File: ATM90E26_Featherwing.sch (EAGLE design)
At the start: 60 parts, among them J1 ST-PJ-312, J2 4P-SMD-2.0-90D, J3 4P-SMD-2.0-90D, J4 12V AC, Q1 8.192MHz, U1 ATM90E26, U2 CJT1117-5.0-SOT223

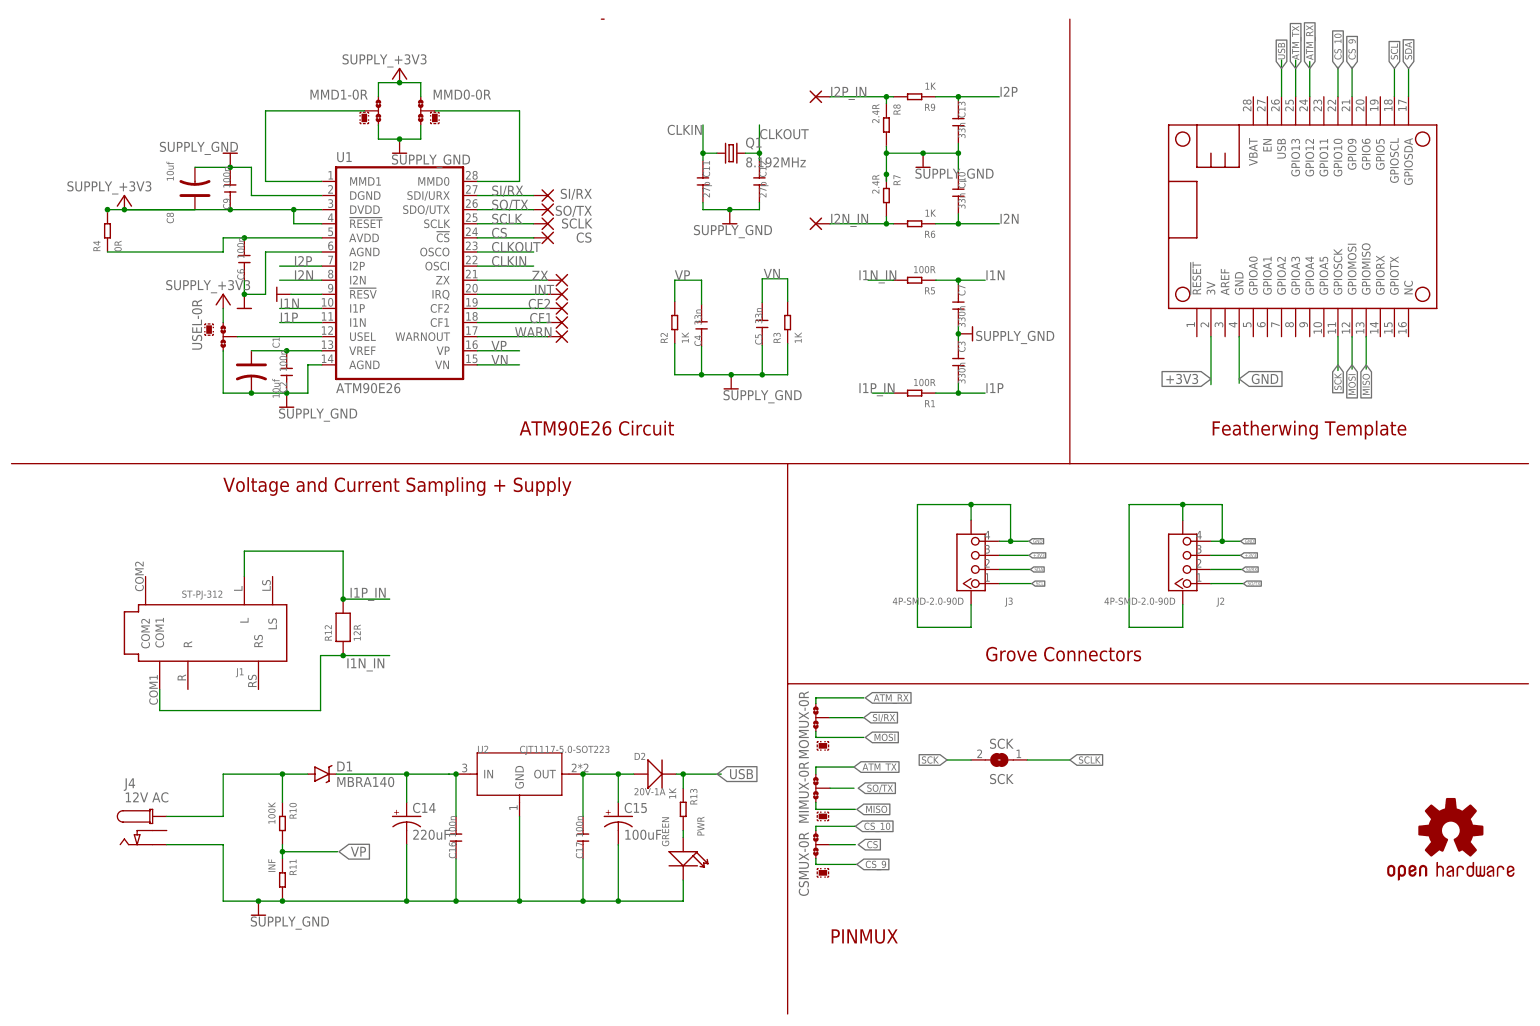
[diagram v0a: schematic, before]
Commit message: Used smaller solder jumpers and finished route, bumped version
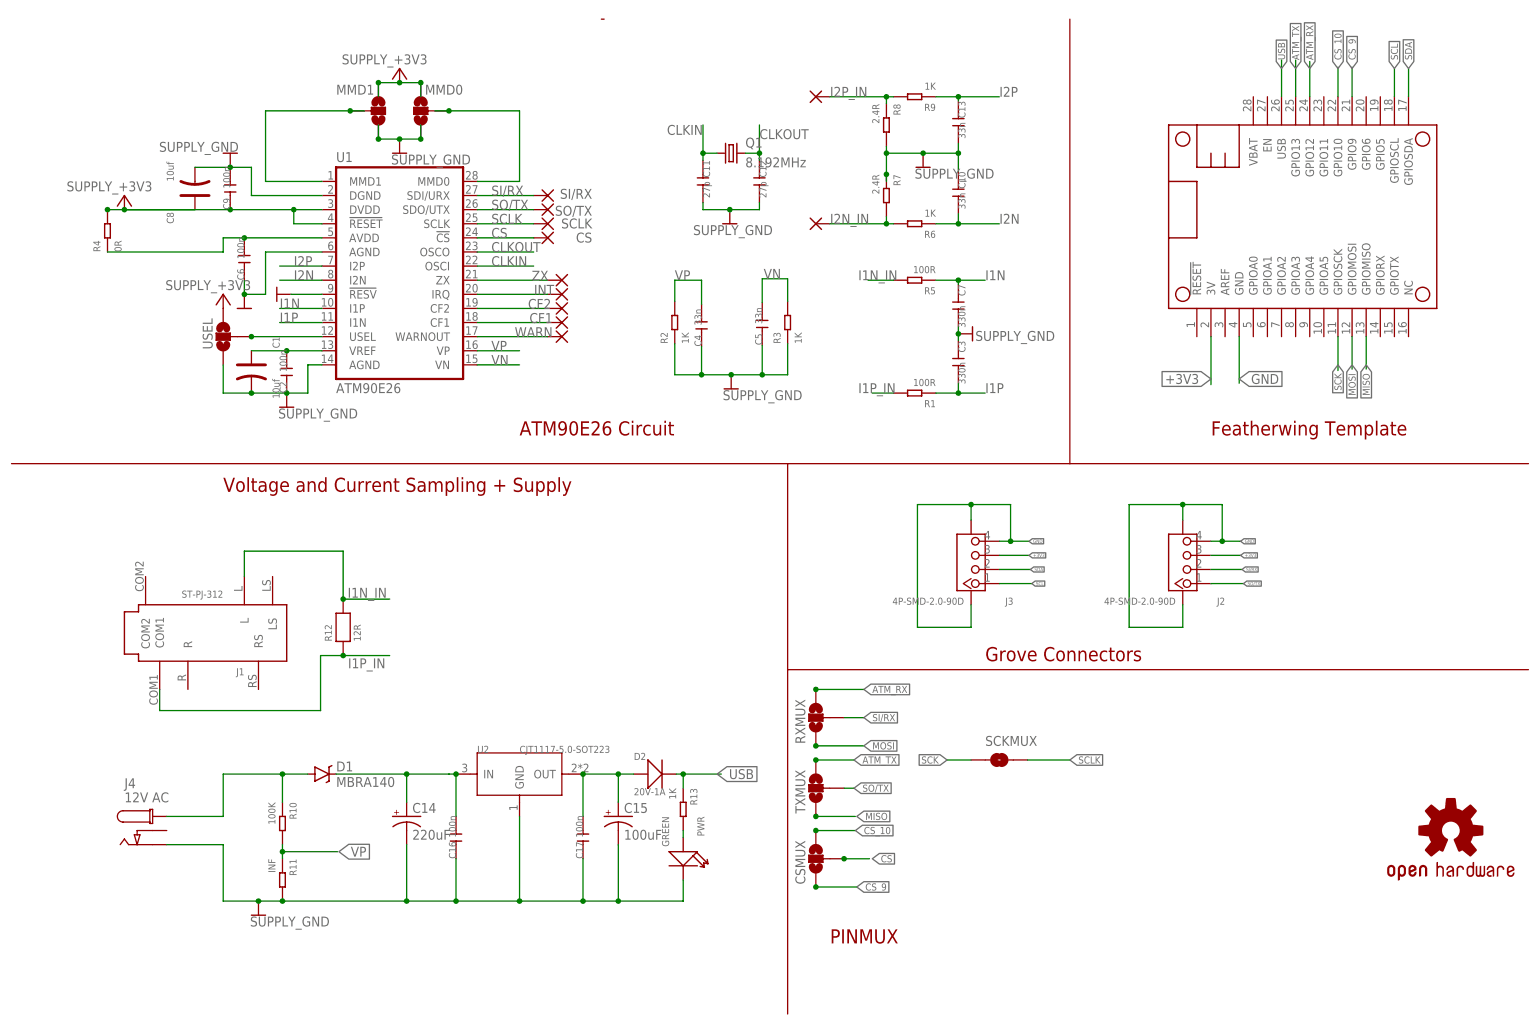
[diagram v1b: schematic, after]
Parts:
- removed MIMUX, MOMUX: 0R-JUMPA, jump-0r-smd:0R-JUMPA
- removed SCK: SCK, jumper:SJ
- added RXMUX, TXMUX: JUMPER-PAD-3-NOYES_SILK, SparkFun-Passives:JUMPER-PAD-3-NOYES_SILK
- added SCKMUX: JUMPER-PAD-2-NOYES_SILK, SparkFun-Passives:JUMPER-PAD-2-NOYES_SILK
- CSMUX: value 0R-JUMPA -> JUMPER-PAD-3-NOYES_SILK; device jump-0r-smd:0R-JUMPA -> SparkFun-Passives:JUMPER-PAD-3-NOYES_SILK
- MMD0, MMD1, USEL: value 0R-JUMPA -> JUMPER-PAD-3-NOFULL_BOX_SILK; device jump-0r-smd:0R-JUMPA -> SparkFun-Passives:JUMPER-PAD-3-NOFULL_BOX_SILK
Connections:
- net +3V3: now also MMD0.3, MMD1.1, USEL.3; no longer MMD0-0R.1, MMD1-0R.3, USEL-0R.1
- net ATM_RX: now also RXMUX.3; no longer MOMUX-0R.1
- net ATM_TX: now also TXMUX.3; no longer MIMUX-0R.1
- net CS: now also CSMUX.2; no longer CSMUX-0R.2
- net CS_10: now also CSMUX.3; no longer CSMUX-0R.1
- net CS_9: now also CSMUX.1; no longer CSMUX-0R.3
- net GND: now also MMD0.1, MMD1.3, USEL.1; no longer MMD0-0R.3, MMD1-0R.1, USEL-0R.3
- net I1N_IN: now also J1.L, R12.2; no longer J1.COM1, R12.1
- net I1P_IN: now also J1.COM1, R12.1; no longer J1.L, R12.2
- net MISO: now also TXMUX.1; no longer MIMUX-0R.3
- net MOSI: now also RXMUX.1; no longer MOMUX-0R.3
- net N$1: now also MMD1.2; no longer MMD1-0R.2
- net N$15: now also USEL.2; no longer USEL-0R.2
- net N$2: now also MMD0.2; no longer MMD0-0R.2
- net SCK: now also SCKMUX.1; no longer SCK.2
- net SCLK: now also SCKMUX.2; no longer SCK.1
- net SI/RX: now also RXMUX.2; no longer MOMUX-0R.2
- net SO/TX: now also TXMUX.2; no longer MIMUX-0R.2

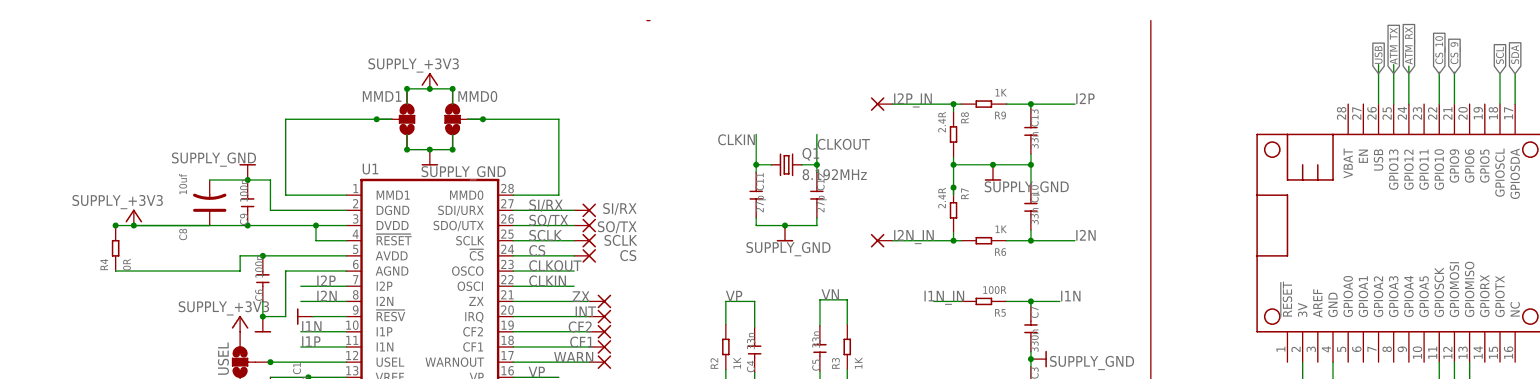
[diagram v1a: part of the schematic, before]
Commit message: Rerouted to new UART pins
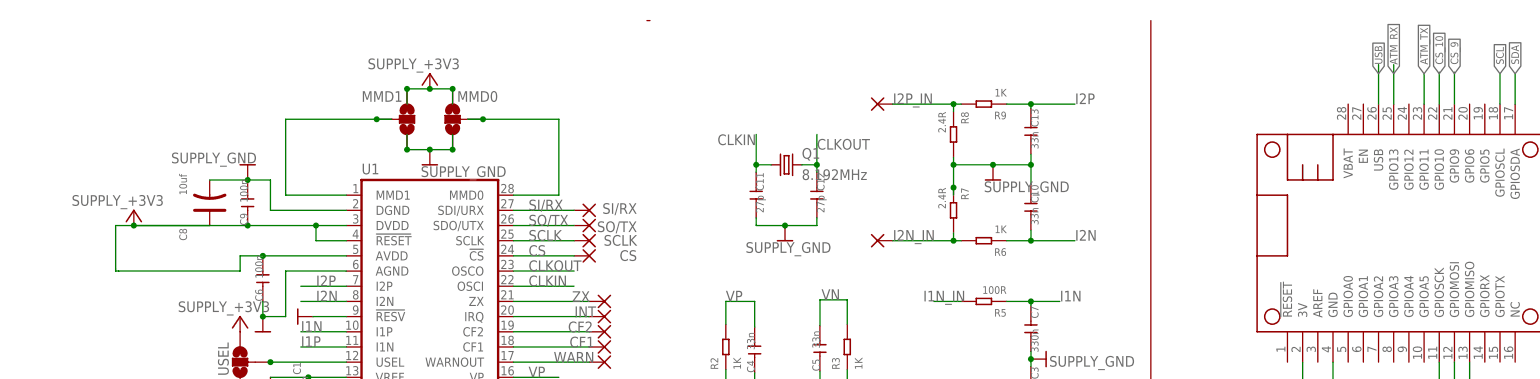
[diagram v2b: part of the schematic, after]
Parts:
- removed R4: 0R, Seeed-Resistor-2016:SMD-RES-0R(0603)
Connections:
- removed net N$6: C6.2, R4.1, U1.AVDD
- net +3V3: now also C6.2, U1.AVDD; no longer R4.2
- net ATM_RX: now also MS1.GPIO13; no longer MS1.GPIO12
- net ATM_TX: now also MS1.GPIO11; no longer MS1.GPIO13
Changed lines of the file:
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@@
 <grid distance="0.1" unitdist="inch" unit="inch" style="lines" multiple="1" display="no" altdistance="0.01" altunitdist="inch" altunit="inch"/>
 <layers>
-<layer number="1" name="Top" color="4" fill="1" visible="yes" active="no"/>
-<layer number="2" name="Route2" color="1" fill="3" visible="yes" active="no"/>
-<layer number="15" name="Route15" color="4" fill="6" visible="yes" active="no"/>
-<layer number="16" name="Bottom" color="1" fill="1" visible="yes" active="no"/>
-<layer number="17" name="Pads" color="2" fill="1" visible="yes" active="no"/>
-<layer number="18" name="Vias" color="2" fill="1" visible="yes" active="no"/>
-<layer number="19" name="Unrouted" color="6" fill="1" visible="yes" active="no"/>
-<layer number="20" name="Dimension" color="15" fill="1" visible="yes" active="no"/>
-<layer number="21" name="tPlace" color="7" fill="1" visible="yes" active="no"/>
-<layer number="22" name="bPlace" color="13" fill="1" visible="yes" active="no"/>
-<layer number="23" name="tOrigins" color="15" fill="1" visible="yes" active="no"/>
-<layer number="24" name="bOrigins" color="15" fill="1" visible="yes" active="no"/>
-<layer number="25" name="tNames" color="7" fill="1" visible="yes" active="no"/>
-<layer number="26" name="bNames" color="13" fill="1" visible="yes" active="no"/>
-<layer number="27" name="tValues" color="7" fill="1" visible="yes" active="no"/>
-<layer number="28" name="bValues" color="7" fill="1" visible="yes" active="no"/>
+<layer number="1" name="Top" color="4" fill="1" visible="no" active="no"/>
+<layer number="2" name="Route2" color="1" fill="3" visible="no" active="no"/>
+<layer number="15" name="Route15" color="4" fill="6" visible="no" active="no"/>
+<layer number="16" name="Bottom" color="1" fill="1" visible="no" active="no"/>
+<layer number="17" name="Pads" color="2" fill="1" visible="no" active="no"/>
+<layer number="18" name="Vias" color="2" fill="1" visible="no" active="no"/>
+<layer number="19" name="Unrouted" color="6" fill="1" visible="no" active="no"/>
+<layer number="20" name="Dimension" color="15" fill="1" visible="no" active="no"/>
+<layer number="21" name="tPlace" color="7" fill="1" visible="no" active="no"/>
+<layer number="22" name="bPlace" color="13" fill="1" visible="no" active="no"/>
+<layer number="23" name="tOrigins" color="15" fill="1" visible="no" active="no"/>
+<layer number="24" name="bOrigins" color="15" fill="1" visible="no" active="no"/>
+<layer number="25" name="tNames" color="7" fill="1" visible="no" active="no"/>
+<layer number="26" name="bNames" color="13" fill="1" visible="no" active="no"/>
+<layer number="27" name="tValues" color="7" fill="1" visible="no" active="no"/>
+<layer number="28" name="bValues" color="7" fill="1" visible="no" active="no"/>
 <layer number="29" name="tStop" color="7" fill="3" visible="no" active="no"/>
 <layer number="30" name="bStop" color="7" fill="6" visible="no" active="no"/>
@@
 <layer number="35" name="tGlue" color="7" fill="4" visible="no" active="no"/>
 <layer number="36" name="bGlue" color="7" fill="5" visible="no" active="no"/>
-<layer number="37" name="tTest" color="7" fill="1" visible="yes" active="no"/>
-<layer number="38" name="bTest" color="7" fill="1" visible="yes" active="no"/>
+<layer number="37" name="tTest" color="7" fill="1" visible="no" active="no"/>
+<layer number="38" name="bTest" color="7" fill="1" visible="no" active="no"/>
 <layer number="39" name="tKeepout" color="4" fill="11" visible="no" active="no"/>
 <layer number="40" name="bKeepout" color="1" fill="11" visible="no" active="no"/>
@@
 <layer number="44" name="Drills" color="7" fill="1" visible="no" active="no"/>
 <layer number="45" name="Holes" color="7" fill="1" visible="no" active="no"/>
-<layer number="46" name="Milling" color="3" fill="1" visible="yes" active="no"/>
-<layer number="47" name="Measures" color="7" fill="1" visible="yes" active="no"/>
-<layer number="48" name="Document" color="7" fill="1" visible="yes" active="no"/>
-<layer number="49" name="Reference" color="7" fill="1" visible="yes" active="no"/>
-<layer number="50" name="dxf" color="7" fill="1" visible="yes" active="no"/>
-<layer number="51" name="tDocu" color="7" fill="1" visible="yes" active="no"/>
-<layer number="52" name="bDocu" color="7" fill="1" visible="yes" active="no"/>
-<layer number="53" name="tGND_GNDA" color="7" fill="9" visible="yes" active="no"/>
-<layer number="54" name="bGND_GNDA" color="1" fill="9" visible="yes" active="no"/>
-<layer number="56" name="wert" color="7" fill="1" visible="yes" active="no"/>
-<layer number="57" name="tCAD" color="7" fill="1" visible="yes" active="no"/>
-<layer number="59" name="tCarbon" color="7" fill="1" visible="yes" active="no"/>
-<layer number="60" name="bCarbon" color="7" fill="1" visible="yes" active="no"/>
+<layer number="46" name="Milling" color="3" fill="1" visible="no" active="no"/>
+<layer number="47" name="Measures" color="7" fill="1" visible="no" active="no"/>
+<layer number="48" name="Document" color="7" fill="1" visible="no" active="no"/>
+<layer number="49" name="Reference" color="7" fill="1" visible="no" active="no"/>
+<layer number="50" name="dxf" color="7" fill="1" visible="no" active="no"/>
+<layer number="51" name="tDocu" color="7" fill="1" visible="no" active="no"/>
+<layer number="52" name="bDocu" color="7" fill="1" visible="no" active="no"/>
+<layer number="53" name="tGND_GNDA" color="7" fill="9" visible="no" active="no"/>
+<layer number="54" name="bGND_GNDA" color="1" fill="9" visible="no" active="no"/>
+<layer number="56" name="wert" color="7" fill="1" visible="no" active="no"/>
+<layer number="57" name="tCAD" color="7" fill="1" visible="no" active="no"/>
+<layer number="59" name="tCarbon" color="7" fill="1" visible="no" active="no"/>
+<layer number="60" name="bCarbon" color="7" fill="1" visible="no" active="no"/>
 <layer number="90" name="Modules" color="5" fill="1" visible="yes" active="yes"/>
 <layer number="91" name="Nets" color="2" fill="1" visible="yes" active="yes"/>
@@
 <part name="C2" library="Discrete" deviceset="C*" device="-0603" value="100n"/>
 <part name="C9" library="Discrete" deviceset="C*" device="-0603" value="100n"/>
-<part name="R4" library="Seeed-Resistor-2016" deviceset="SMD-RES-0R(0603)" device="" value="0R"/>
 <part name="C6" library="Discrete" deviceset="C*" device="-0603" value="100n"/>
 <part name="GND1" library="dp_devices" deviceset="SUPPLY_GND" device=""/>
@@
 <instance part="C2" gate="C" x="11.43" y="39.37" rot="R90"/>
 <instance part="C9" gate="C" x="1.27" y="72.39" rot="R90"/>
-<instance part="R4" gate="G$1" x="-20.828" y="64.77" smashed="yes" rot="R90">
-<attribute name="NAME" x="-22.098" y="60.96" size="1.27" layer="95" ratio="10" rot="R90"/>
-<attribute name="VALUE" x="-18.288" y="60.96" size="1.27" layer="96" ratio="10" rot="R90"/>
-</instance>
 <instance part="C6" gate="C" x="3.81" y="59.69" rot="R90"/>
 <instance part="GND1" gate="G$1" x="3.81" y="50.8" smashed="yes"/>
@@
 <wire x1="40.64" y1="86.36" x2="38.1" y2="86.36" width="0.1524" layer="91"/>
 <junction x="40.64" y="86.36"/>
-</segment>
-</net>
-<net name="N$6" class="1">
-<segment>
-<pinref part="U1" gate="G$1" pin="AVDD"/>
-<wire x1="17.78" y1="63.5" x2="3.81" y2="63.5" width="0.1524" layer="91"/>
-<wire x1="3.81" y1="63.5" x2="0" y2="63.5" width="0.1524" layer="91"/>
-<wire x1="0" y1="60.96" x2="0" y2="63.5" width="0.1524" layer="91"/>
-<wire x1="-20.828" y1="60.96" x2="0" y2="60.96" width="0.1524" layer="91"/>
-<pinref part="R4" gate="G$1" pin="1"/>
-<pinref part="C6" gate="C" pin="2"/>
-<junction x="3.81" y="63.5"/>
 </segment>
 </net>
@@
 <pinref part="C9" gate="C" pin="1"/>
 <junction x="1.27" y="68.58"/>
-<pinref part="R4" gate="G$1" pin="2"/>
-<junction x="-20.828" y="68.58"/>
 <pinref part="+3V1" gate="G$1" pin="+3V3"/>
 <junction x="-17.78" y="68.58"/>
+<wire x1="-20.828" y1="68.58" x2="-20.828" y2="61.468" width="0.1524" layer="91"/>
+<pinref part="U1" gate="G$1" pin="AVDD"/>
+<wire x1="-20.828" y1="61.468" x2="-20.828" y2="61.214" width="0.1524" layer="91"/>
+<wire x1="17.78" y1="63.5" x2="3.81" y2="63.5" width="0.1524" layer="91"/>
+<wire x1="3.81" y1="63.5" x2="0" y2="63.5" width="0.1524" layer="91"/>
+<wire x1="0" y1="60.96" x2="0" y2="63.5" width="0.1524" layer="91"/>
+<pinref part="C6" gate="C" pin="2"/>
+<junction x="3.81" y="63.5"/>
+<wire x1="-20.32" y1="60.96" x2="0" y2="60.96" width="0.1524" layer="91"/>
+<wire x1="-20.32" y1="60.96" x2="-20.828" y2="60.96" width="0.1524" layer="91"/>
+<wire x1="-20.828" y1="60.96" x2="-20.828" y2="61.214" width="0.1524" layer="91"/>
 </segment>
 <segment>
@@
 <net name="ATM_TX" class="0">
 <segment>
-<pinref part="MS1" gate="G$1" pin="GPIO13"/>
-<wire x1="193.04" y1="88.9" x2="193.04" y2="95.504" width="0.1524" layer="91"/>
-<label x="193.04" y="93.98" size="1.27" layer="95" rot="R90" xref="yes"/>
-</segment>
-<segment>
 <wire x1="106.68" y1="-30.48" x2="113.538" y2="-30.48" width="0.1524" layer="91"/>
 <label x="113.538" y="-30.48" size="1.27" layer="95" xref="yes"/>
@@
 <junction x="106.68" y="-30.48"/>
 </segment>
+<segment>
+<pinref part="MS1" gate="G$1" pin="GPIO11"/>
+<wire x1="198.12" y1="88.9" x2="198.12" y2="93.98" width="0.1524" layer="91"/>
+<label x="198.12" y="93.98" size="1.27" layer="95" rot="R90" xref="yes"/>
+</segment>
 </net>
 <net name="ATM_RX" class="0">
-<segment>
-<pinref part="MS1" gate="G$1" pin="GPIO12"/>
-<wire x1="195.58" y1="88.9" x2="195.58" y2="95.25" width="0.1524" layer="91"/>
-<label x="195.58" y="93.98" size="1.27" layer="95" rot="R90" xref="yes"/>
-</segment>
 <segment>
 <wire x1="106.68" y1="-17.78" x2="115.316" y2="-17.78" width="0.1524" layer="91"/>
@@
 <junction x="106.68" y="-17.78"/>
 </segment>
-</net>
+<segment>
+<pinref part="MS1" gate="G$1" pin="GPIO13"/>
+<wire x1="193.04" y1="88.9" x2="193.04" y2="95.504" width="0.1524" layer="91"/>
+<label x="193.04" y="93.98" size="1.27" layer="95" rot="R90" xref="yes"/>
+</segment>
+</net>
